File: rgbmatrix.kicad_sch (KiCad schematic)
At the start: 164 parts

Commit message: first
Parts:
- C10: renamed from C2; footprint (none) -> Capacitor_SMD:C_0805_2012Metric_Pad1.18x1.45mm_HandSolder
- C11: renamed from C3; footprint (none) -> Capacitor_SMD:C_0805_2012Metric_Pad1.18x1.45mm_HandSolder
- C12: renamed from C4; footprint (none) -> Capacitor_SMD:C_0805_2012Metric_Pad1.18x1.45mm_HandSolder
- C13: renamed from C5; footprint (none) -> Capacitor_SMD:C_0805_2012Metric_Pad1.18x1.45mm_HandSolder
- C14: renamed from C6; footprint (none) -> Capacitor_SMD:C_0805_2012Metric_Pad1.18x1.45mm_HandSolder
- C15: renamed from C7; footprint (none) -> Capacitor_SMD:C_0805_2012Metric_Pad1.18x1.45mm_HandSolder
- C16: renamed from C8; footprint (none) -> Capacitor_SMD:C_0805_2012Metric_Pad1.18x1.45mm_HandSolder
- C17: renamed from C9; footprint (none) -> Capacitor_SMD:C_0805_2012Metric_Pad1.18x1.45mm_HandSolder
- C18: renamed from C10; footprint (none) -> Capacitor_SMD:C_0805_2012Metric_Pad1.18x1.45mm_HandSolder
- C19: renamed from C11; footprint (none) -> Capacitor_SMD:C_0805_2012Metric_Pad1.18x1.45mm_HandSolder
- C20: renamed from C12; footprint (none) -> Capacitor_SMD:C_0805_2012Metric_Pad1.18x1.45mm_HandSolder
- C21: renamed from C13; footprint (none) -> Capacitor_SMD:C_0805_2012Metric_Pad1.18x1.45mm_HandSolder
- C22: renamed from C14; footprint (none) -> Capacitor_SMD:C_0805_2012Metric_Pad1.18x1.45mm_HandSolder
- C23: renamed from C15; footprint (none) -> Capacitor_SMD:C_0805_2012Metric_Pad1.18x1.45mm_HandSolder
- C24: renamed from C16; footprint (none) -> Capacitor_SMD:C_0805_2012Metric_Pad1.18x1.45mm_HandSolder
- C25: renamed from C17; footprint (none) -> Capacitor_SMD:C_0805_2012Metric_Pad1.18x1.45mm_HandSolder
- C26: renamed from C18; footprint (none) -> Capacitor_SMD:C_0805_2012Metric_Pad1.18x1.45mm_HandSolder
- C27: renamed from C19; footprint (none) -> Capacitor_SMD:C_0805_2012Metric_Pad1.18x1.45mm_HandSolder
- C28: renamed from C20; footprint (none) -> Capacitor_SMD:C_0805_2012Metric_Pad1.18x1.45mm_HandSolder
- C29: renamed from C21; footprint (none) -> Capacitor_SMD:C_0805_2012Metric_Pad1.18x1.45mm_HandSolder
- C30: renamed from C22; footprint (none) -> Capacitor_SMD:C_0805_2012Metric_Pad1.18x1.45mm_HandSolder
- C31: renamed from C23; footprint (none) -> Capacitor_SMD:C_0805_2012Metric_Pad1.18x1.45mm_HandSolder
- C32: renamed from C24; footprint (none) -> Capacitor_SMD:C_0805_2012Metric_Pad1.18x1.45mm_HandSolder
- C33: renamed from C25; footprint (none) -> Capacitor_SMD:C_0805_2012Metric_Pad1.18x1.45mm_HandSolder
- C34: renamed from C26; footprint (none) -> Capacitor_SMD:C_0805_2012Metric_Pad1.18x1.45mm_HandSolder
- C35: renamed from C27; footprint (none) -> Capacitor_SMD:C_0805_2012Metric_Pad1.18x1.45mm_HandSolder
- C36: renamed from C28; footprint (none) -> Capacitor_SMD:C_0805_2012Metric_Pad1.18x1.45mm_HandSolder
- C37: renamed from C29; footprint (none) -> Capacitor_SMD:C_0805_2012Metric_Pad1.18x1.45mm_HandSolder
- C38: renamed from C30; footprint (none) -> Capacitor_SMD:C_0805_2012Metric_Pad1.18x1.45mm_HandSolder
- C39: renamed from C31; footprint (none) -> Capacitor_SMD:C_0805_2012Metric_Pad1.18x1.45mm_HandSolder
- C40: renamed from C32; footprint (none) -> Capacitor_SMD:C_0805_2012Metric_Pad1.18x1.45mm_HandSolder
- C41: renamed from C33; footprint (none) -> Capacitor_SMD:C_0805_2012Metric_Pad1.18x1.45mm_HandSolder
- C42: renamed from C34; footprint (none) -> Capacitor_SMD:C_0805_2012Metric_Pad1.18x1.45mm_HandSolder
- C43: renamed from C35; footprint (none) -> Capacitor_SMD:C_0805_2012Metric_Pad1.18x1.45mm_HandSolder
- C44: renamed from C36; footprint (none) -> Capacitor_SMD:C_0805_2012Metric_Pad1.18x1.45mm_HandSolder
- C45: renamed from C37; footprint (none) -> Capacitor_SMD:C_0805_2012Metric_Pad1.18x1.45mm_HandSolder
- C46: renamed from C38; footprint (none) -> Capacitor_SMD:C_0805_2012Metric_Pad1.18x1.45mm_HandSolder
- C47: renamed from C39; footprint (none) -> Capacitor_SMD:C_0805_2012Metric_Pad1.18x1.45mm_HandSolder
- C48: renamed from C40; footprint (none) -> Capacitor_SMD:C_0805_2012Metric_Pad1.18x1.45mm_HandSolder
- C49: renamed from C41; footprint (none) -> Capacitor_SMD:C_0805_2012Metric_Pad1.18x1.45mm_HandSolder
- C50: renamed from C42; footprint (none) -> Capacitor_SMD:C_0805_2012Metric_Pad1.18x1.45mm_HandSolder
- C51: renamed from C43; footprint (none) -> Capacitor_SMD:C_0805_2012Metric_Pad1.18x1.45mm_HandSolder
- C52: renamed from C44; footprint (none) -> Capacitor_SMD:C_0805_2012Metric_Pad1.18x1.45mm_HandSolder
- C53: renamed from C45; footprint (none) -> Capacitor_SMD:C_0805_2012Metric_Pad1.18x1.45mm_HandSolder
- C54: renamed from C46; footprint (none) -> Capacitor_SMD:C_0805_2012Metric_Pad1.18x1.45mm_HandSolder
- C55: renamed from C47; footprint (none) -> Capacitor_SMD:C_0805_2012Metric_Pad1.18x1.45mm_HandSolder
- C56: renamed from C48; footprint (none) -> Capacitor_SMD:C_0805_2012Metric_Pad1.18x1.45mm_HandSolder
- C57: renamed from C49; footprint (none) -> Capacitor_SMD:C_0805_2012Metric_Pad1.18x1.45mm_HandSolder
- C58: renamed from C50; footprint (none) -> Capacitor_SMD:C_0805_2012Metric_Pad1.18x1.45mm_HandSolder
- C59: renamed from C51; footprint (none) -> Capacitor_SMD:C_0805_2012Metric_Pad1.18x1.45mm_HandSolder
- C60: renamed from C52; footprint (none) -> Capacitor_SMD:C_0805_2012Metric_Pad1.18x1.45mm_HandSolder
- C61: renamed from C53; footprint (none) -> Capacitor_SMD:C_0805_2012Metric_Pad1.18x1.45mm_HandSolder
- C62: renamed from C54; footprint (none) -> Capacitor_SMD:C_0805_2012Metric_Pad1.18x1.45mm_HandSolder
- C63: renamed from C55; footprint (none) -> Capacitor_SMD:C_0805_2012Metric_Pad1.18x1.45mm_HandSolder
- C64: renamed from C56; footprint (none) -> Capacitor_SMD:C_0805_2012Metric_Pad1.18x1.45mm_HandSolder
- C65: renamed from C57; footprint (none) -> Capacitor_SMD:C_0805_2012Metric_Pad1.18x1.45mm_HandSolder
- C66: renamed from C58; footprint (none) -> Capacitor_SMD:C_0805_2012Metric_Pad1.18x1.45mm_HandSolder
- C67: renamed from C59; footprint (none) -> Capacitor_SMD:C_0805_2012Metric_Pad1.18x1.45mm_HandSolder
- C68: renamed from C60; footprint (none) -> Capacitor_SMD:C_0805_2012Metric_Pad1.18x1.45mm_HandSolder
- C69: renamed from C61; footprint (none) -> Capacitor_SMD:C_0805_2012Metric_Pad1.18x1.45mm_HandSolder
- C70: renamed from C62; footprint (none) -> Capacitor_SMD:C_0805_2012Metric_Pad1.18x1.45mm_HandSolder
- C71: renamed from C63; footprint (none) -> Capacitor_SMD:C_0805_2012Metric_Pad1.18x1.45mm_HandSolder
- C72: renamed from C64; footprint (none) -> Capacitor_SMD:C_0805_2012Metric_Pad1.18x1.45mm_HandSolder
- C73: renamed from C65; footprint (none) -> Capacitor_SMD:C_0805_2012Metric_Pad1.18x1.45mm_HandSolder
- C74: renamed from C66; footprint (none) -> Capacitor_SMD:C_0805_2012Metric_Pad1.18x1.45mm_HandSolder
- C75: renamed from C67; footprint (none) -> Capacitor_SMD:C_0805_2012Metric_Pad1.18x1.45mm_HandSolder
- C76: renamed from C68; footprint (none) -> Capacitor_SMD:C_0805_2012Metric_Pad1.18x1.45mm_HandSolder
- C77: renamed from C69; footprint (none) -> Capacitor_SMD:C_0805_2012Metric_Pad1.18x1.45mm_HandSolder
- C78: renamed from C70; footprint (none) -> Capacitor_SMD:C_0805_2012Metric_Pad1.18x1.45mm_HandSolder
- C79: renamed from C71; footprint (none) -> Capacitor_SMD:C_0805_2012Metric_Pad1.18x1.45mm_HandSolder
- C80: renamed from C72; footprint (none) -> Capacitor_SMD:C_0805_2012Metric_Pad1.18x1.45mm_HandSolder
- C81: renamed from C73; footprint (none) -> Capacitor_SMD:C_0805_2012Metric_Pad1.18x1.45mm_HandSolder
- C82: renamed from C74; footprint (none) -> Capacitor_SMD:C_0805_2012Metric_Pad1.18x1.45mm_HandSolder
- C83: renamed from C75; footprint (none) -> Capacitor_SMD:C_0805_2012Metric_Pad1.18x1.45mm_HandSolder
- C84: renamed from C76; footprint (none) -> Capacitor_SMD:C_0805_2012Metric_Pad1.18x1.45mm_HandSolder
- C85: renamed from C77; footprint (none) -> Capacitor_SMD:C_0805_2012Metric_Pad1.18x1.45mm_HandSolder
- C86: renamed from C78; footprint (none) -> Capacitor_SMD:C_0805_2012Metric_Pad1.18x1.45mm_HandSolder
- C87: renamed from C79; footprint (none) -> Capacitor_SMD:C_0805_2012Metric_Pad1.18x1.45mm_HandSolder
- C88: renamed from C80; footprint (none) -> Capacitor_SMD:C_0805_2012Metric_Pad1.18x1.45mm_HandSolder
- C89: renamed from C81; footprint (none) -> Capacitor_SMD:C_0805_2012Metric_Pad1.18x1.45mm_HandSolder
- C9: renamed from C1; footprint (none) -> Capacitor_SMD:C_0805_2012Metric_Pad1.18x1.45mm_HandSolder
- C90: renamed from C82; footprint (none) -> Capacitor_SMD:C_0805_2012Metric_Pad1.18x1.45mm_HandSolder
- renumbered D9 to D10, D10 to D11, D11 to D12, D12 to D13, D13 to D14, D14 to D15, D15 to D16, D16 to D17, D17 to D18, D18 to D19, D1 to D2, D19 to D20, D20 to D21, D21 to D22, D22 to D23, D23 to D24, D24 to D25, D25 to D26, D26 to D27, D27 to D28, D28 to D29, D2 to D3, D29 to D30, D30 to D31, D31 to D32, D32 to D33, D33 to D34, D34 to D35, D35 to D36, D36 to D37, D37 to D38, D38 to D39, D3 to D4, D39 to D40, D40 to D41, D41 to D42, D42 to D43, D43 to D44, D44 to D45, D45 to D46, D46 to D47, D47 to D48, D48 to D49, D4 to D5, D49 to D50, D50 to D51, D51 to D52, D52 to D53, D53 to D54, D54 to D55, D55 to D56, D56 to D57, D57 to D58, D58 to D59, D5 to D6, D59 to D60, D60 to D61, D61 to D62, D62 to D63, D63 to D64, D64 to D65, D65 to D66, D66 to D67, D67 to D68, D68 to D69, D6 to D7, D69 to D70, D70 to D71, D71 to D72, D72 to D73, D73 to D74, D74 to D75, D75 to D76, D76 to D77, D77 to D78, D78 to D79, D7 to D8, D79 to D80, D80 to D81, D81 to D82, D82 to D83, D8 to D9
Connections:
- net +5V: now also D82.2 (VSS), D83.2 (VSS)

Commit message: changed to 60 :C
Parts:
- removed C10, C11, C12, C13, C14, C15, C16, C17, C18, C19, C20, C21, C22, C9: 100nF, Capacitor_SMD:C_0805_2012Metric_Pad1.18x1.45mm_HandSolder, symbol Device:C_Small
- removed D10, D11, D12, D13, D14, D15, D2, D3, D4, D5, D6, D7, D8, D9: SK6812MINI, LED_SMD:LED_SK6812MINI_PLCC4_3.5x3.5mm_P1.75mm, symbol LED:SK6812MINI
- renumbered C24 to C10, C25 to C11, C26 to C12, C27 to C13, C28 to C14, C29 to C15, C30 to C16, C31 to C17, C32 to C18, C33 to C19, C34 to C20, C35 to C21, C36 to C22, C37 to C23, C38 to C24, C39 to C25, C40 to C26, C41 to C27, C42 to C28, C43 to C29, C44 to C30, C45 to C31, C46 to C32, C47 to C33, C48 to C34, C49 to C35, C50 to C36, C51 to C37, C52 to C38, C53 to C39, C54 to C40, C55 to C41, C56 to C42, C57 to C43, C58 to C44, C59 to C45, C60 to C46, C61 to C47, C62 to C48, C63 to C49, C64 to C50, C65 to C51, C66 to C52, C67 to C53, C68 to C54, C69 to C55, C70 to C56, C71 to C57, C72 to C58, C73 to C59, C74 to C60, C75 to C61, C76 to C62, C77 to C63, C78 to C64, C79 to C65, C80 to C66, C81 to C67, C82 to C68, C83 to C69, C84 to C70, C85 to C71, C86 to C72, C87 to C73, C88 to C74, C89 to C75, C90 to C76, C23 to C9, D24 to D10, D25 to D11, D26 to D12, D27 to D13, D28 to D14, D29 to D15, D30 to D16, D31 to D17, D32 to D18, D33 to D19, D16 to D2, D34 to D20, D35 to D21, D36 to D22, D37 to D23, D38 to D24, D39 to D25, D40 to D26, D41 to D27, D42 to D28, D43 to D29, D17 to D3, D44 to D30, D45 to D31, D46 to D32, D47 to D33, D48 to D34, D49 to D35, D50 to D36, D51 to D37, D52 to D38, D53 to D39, D18 to D4, D54 to D40, D55 to D41, D56 to D42, D57 to D43, D58 to D44, D59 to D45, D60 to D46, D61 to D47, D62 to D48, D63 to D49, D19 to D5, D64 to D50, D65 to D51, D66 to D52, D67 to D53, D68 to D54, D69 to D55, D70 to D56, D71 to D57, D72 to D58, D73 to D59, D20 to D6, D74 to D60, D75 to D61, D76 to D62, D77 to D63, D78 to D64, D79 to D65, D80 to D66, D81 to D67, D82 to D68, D83 to D69, D21 to D7, D22 to D8, D23 to D9
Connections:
- net D72 is gone; now on net D59: D59.1 (DOUT), D60.3 (DIN)
- net D59: no longer D46.3 (DIN)
- net D14 renamed LED
- net D29 renamed D16
- net D44 renamed D31
- net D58 renamed D45
- net D45: now also D46.3 (DIN)
- net D80: no longer names the net of D67.1 (DOUT), D68.3 (DIN)
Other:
- moved on the sheet: C10, C11, C12, C13, C14, C15, C16, C17, C18, C19, C20, C21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

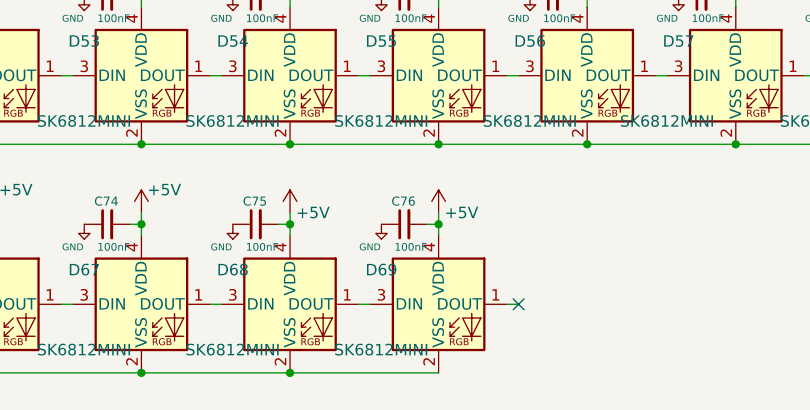
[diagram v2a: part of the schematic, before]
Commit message: moved keys/neopixels
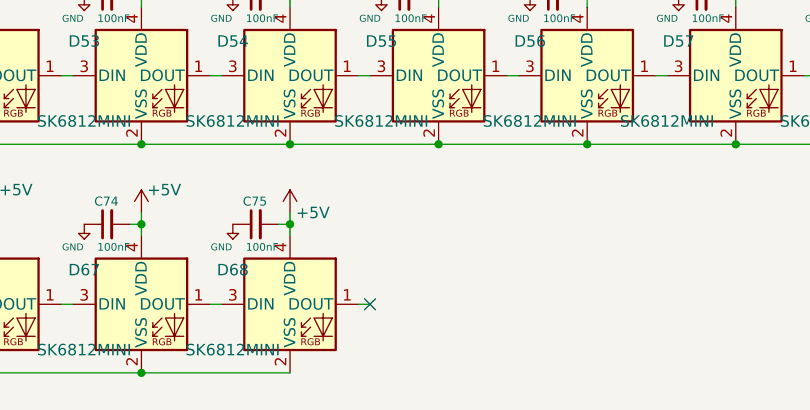
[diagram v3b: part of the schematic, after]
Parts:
- removed C76: 100nF, Capacitor_SMD:C_0805_2012Metric_Pad1.18x1.45mm_HandSolder, symbol Device:C_Small
- removed D69: SK6812MINI, LED_SMD:LED_SK6812MINI_PLCC4_3.5x3.5mm_P1.75mm, symbol LED:SK6812MINI
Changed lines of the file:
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@@
   (junction (at 49.53 69.85) (diameter 0) (color 0 0 0 0)
   )
-  (junction (at 165.1 147.32) (diameter 0) (color 0 0 0 0)
-  )
   (junction (at 49.53 24.13) (diameter 0) (color 0 0 0 0)
   )
@@
   (junction (at 66.04 96.52) (diameter 0) (color 0 0 0 0)
   )
-  (junction (at 181.61 130.81) (diameter 0) (color 0 0 0 0)
-  )
   (junction (at 148.59 40.64) (diameter 0) (color 0 0 0 0)
   )
@@
   (junction (at 214.63 24.13) (diameter 0) (color 0 0 0 0)
   )
-  (no_connect (at 190.5 139.7))
+  (no_connect (at 173.99 139.7))
   (wire (pts (xy 49.53 52.07) (xy 49.53 53.34))
     (stroke (width 0) (type default) (color 0 0 0 0))
@@
     (stroke (width 0) (type default) (color 0 0 0 0))
   )
-  (wire (pts (xy 165.1 147.32) (xy 181.61 147.32))
-    (stroke (width 0) (type default) (color 0 0 0 0))
-  )
   (wire (pts (xy 115.57 22.86) (xy 115.57 24.13))
     (stroke (width 0) (type default) (color 0 0 0 0))
@@
     (stroke (width 0) (type default) (color 0 0 0 0))
   )
-  (wire (pts (xy 180.34 130.81) (xy 181.61 130.81))
-    (stroke (width 0) (type default) (color 0 0 0 0))
-  )
-  (wire (pts (xy 181.61 129.54) (xy 181.61 130.81))
-    (stroke (width 0) (type default) (color 0 0 0 0))
-  )
   (wire (pts (xy 246.38 80.01) (xy 247.65 80.01))
     (stroke (width 0) (type default) (color 0 0 0 0))
@@
     (stroke (width 0) (type default) (color 0 0 0 0))
   )
-  (wire (pts (xy 181.61 130.81) (xy 181.61 132.08))
-    (stroke (width 0) (type default) (color 0 0 0 0))
-  )
   (wire (pts (xy 49.53 147.32) (xy 58.42 147.32))
     (stroke (width 0) (type default) (color 0 0 0 0))
@@
     (stroke (width 0) (type default) (color 0 0 0 0))
   )
-  (wire (pts (xy 189.23 139.7) (xy 190.5 139.7))
-    (stroke (width 0) (type default) (color 0 0 0 0))
-  )
   (wire (pts (xy 247.65 52.07) (xy 247.65 53.34))
     (stroke (width 0) (type default) (color 0 0 0 0))
@@
     (pin "1")
   )
-  (symbol (lib_id "keyboard_parts:GND") (at 175.26 130.81 0) (unit 1)
-    (in_bom yes) (on_board yes)
-    (property "Reference" "#PWR0157" (id 0) (at 175.26 129.54 0)
-      (effects (font (size 0.508 0.508)) hide)
-    )
-    (property "Value" "GND" (id 1) (at 173.99 133.35 0)
-      (effects (font (size 0.762 0.762)))
-    )
-    (property "Footprint" "" (id 2) (at 175.26 130.81 0)
-      (effects (font (size 1.524 1.524)))
-    )
-    (property "Datasheet" "" (id 3) (at 175.26 130.81 0)
-      (effects (font (size 1.524 1.524)))
-    )
-    (pin "1")
-  )
   (symbol (lib_id "Device:C_Small") (at 161.29 24.13 90) (unit 1)
     (in_bom yes) (on_board yes)
@@
     (pin "4")
   )
-  (symbol (lib_id "Device:C_Small") (at 177.8 130.81 90) (unit 1)
-    (in_bom yes) (on_board yes)
-    (property "Reference" "C76" (id 0) (at 179.07 128.27 90)
-      (effects (font (size 1 1)) (justify left))
-    )
-    (property "Value" "100nF" (id 1) (at 180.34 133.35 90)
-      (effects (font (size 0.85 0.85)) (justify left))
-    )
-    (property "Footprint" "Capacitor_SMD:C_0805_2012Metric_Pad1.18x1.45mm_HandSolder" (id 2) (at 177.8 130.81 0)
-      (effects (font (size 1.27 1.27)) hide)
-    )
-    (property "Datasheet" "~" (id 3) (at 177.8 130.81 0)
-      (effects (font (size 1.27 1.27)) hide)
-    )
-    (pin "1")
-    (pin "2")
-  )
   (symbol (lib_id "keyboard_parts:GND") (at 241.3 53.34 0) (unit 1)
     (in_bom yes) (on_board yes)
@@
     (pin "1")
   )
-  (symbol (lib_id "power:+5V") (at 181.61 129.54 0) (unit 1)
-    (in_bom yes) (on_board yes)
-    (property "Reference" "#PWR0147" (id 0) (at 181.61 133.35 0)
-      (effects (font (size 1.27 1.27)) hide)
-    )
-    (property "Value" "+5V" (id 1) (at 184.15 129.54 0))
-    (property "Footprint" "" (id 2) (at 181.61 129.54 0)
-      (effects (font (size 1.27 1.27)) hide)
-    )
-    (property "Datasheet" "" (id 3) (at 181.61 129.54 0)
-      (effects (font (size 1.27 1.27)) hide)
-    )
-    (pin "1")
-  )
   (symbol (lib_id "Device:C_Small") (at 29.21 24.13 90) (unit 1)
     (in_bom yes) (on_board yes)
@@
     (pin "1")
   )
-  (symbol (lib_id "LED:SK6812MINI") (at 181.61 139.7 0) (unit 1)
-    (in_bom yes) (on_board yes)
-    (property "Reference" "D69" (id 0) (at 175.26 135.89 0))
-    (property "Value" "SK6812MINI" (id 1) (at 175.26 144.78 0))
-    (property "Footprint" "LED_SMD:LED_SK6812MINI_PLCC4_3.5x3.5mm_P1.75mm" (id 2) (at 182.88 147.32 0)
-      (effects (font (size 1.27 1.27)) (justify left top) hide)
-    )
-    (property "Datasheet" "https://cdn-shop.adafruit.com/product-files/2686/SK6812MINI_REV.01-1-2.pdf" (id 3) (at 184.15 149.225 0)
-      (effects (font (size 1.27 1.27)) (justify left top) hide)
-    )
-    (pin "1")
-    (pin "2")
-    (pin "3")
-    (pin "4")
-  )
   (symbol (lib_id "Device:C_Small") (at 111.76 105.41 90) (unit 1)

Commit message: began routing for real
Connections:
- net +5V: no longer C10.1, C11.1, C12.1, C13.1, C14.1, C15.1, C16.1, C17.1, C18.1, C19.1, C20.1, C21.1, C22.1, C23.1, C24.1, C25.1, C26.1, C27.1, C28.1, C29.1, C30.1, C31.1, C32.1, C33.1, C34.1, C35.1, C36.1, C37.1, C38.1, C39.1, C40.1, C41.1, C42.1, C43.1, C44.1, C45.1, C46.1, C47.1, C48.1, C49.1, C50.1, C51.1, C52.1, C53.1, C54.1, C55.1, C56.1, C57.1, C58.1, C59.1, C60.1, C61.1, C62.1, C63.1, C64.1, C65.1, C66.1, C67.1, C68.1, C69.1, C70.1, C71.1, C72.1, C73.1, C74.1, C75.1, C9.1, D10.2 (VSS), D11.2 (VSS), D12.2 (VSS), D13.2 (VSS), D14.2 (VSS), D15.2 (VSS), D16.2 (VSS), D17.2 (VSS), D18.2 (VSS), D19.2 (VSS), D2.2 (VSS), D20.2 (VSS), D21.2 (VSS), D22.2 (VSS), D23.2 (VSS), D24.2 (VSS), D25.2 (VSS), D26.2 (VSS), D27.2 (VSS), D28.2 (VSS), D29.2 (VSS), D3.2 (VSS), D30.2 (VSS), D31.2 (VSS), D32.2 (VSS), D33.2 (VSS), D34.2 (VSS), D35.2 (VSS), D36.2 (VSS), D37.2 (VSS), D38.2 (VSS), D39.2 (VSS), D4.2 (VSS), D40.2 (VSS), D41.2 (VSS), D42.2 (VSS), D43.2 (VSS), D44.2 (VSS), D45.2 (VSS), D46.2 (VSS), D47.2 (VSS), D48.2 (VSS), D49.2 (VSS), D5.2 (VSS), D50.2 (VSS), D51.2 (VSS), D52.2 (VSS), D53.2 (VSS), D54.2 (VSS), D55.2 (VSS), D56.2 (VSS), D57.2 (VSS), D58.2 (VSS), D59.2 (VSS), D6.2 (VSS), D60.2 (VSS), D61.2 (VSS), D62.2 (VSS), D63.2 (VSS), D64.2 (VSS), D65.2 (VSS), D66.2 (VSS), D67.2 (VSS), D68.2 (VSS), D7.2 (VSS), D8.2 (VSS), D9.2 (VSS)
- new net GND: C10.1, C11.1, C12.1, C13.1, C14.1, C15.1, C16.1, C17.1, C18.1, C19.1, C20.1, C21.1, C22.1, C23.1, C24.1, C25.1, C26.1, C27.1, C28.1, C29.1, C30.1, C31.1, C32.1, C33.1, C34.1, C35.1, C36.1, C37.1, C38.1, C39.1, C40.1, C41.1, C42.1, C43.1, C44.1, C45.1, C46.1, C47.1, C48.1, C49.1, C50.1, C51.1, C52.1, C53.1, C54.1, C55.1, C56.1, C57.1, C58.1, C59.1, C60.1, C61.1, C62.1, C63.1, C64.1, C65.1, C66.1, C67.1, C68.1, C69.1, C70.1, C71.1, C72.1, C73.1, C74.1, C75.1, C9.1, D10.2 (VSS), D11.2 (VSS), D12.2 (VSS), D13.2 (VSS), D14.2 (VSS), D15.2 (VSS), D16.2 (VSS), D17.2 (VSS), D18.2 (VSS), D19.2 (VSS), D2.2 (VSS), D20.2 (VSS), D21.2 (VSS), D22.2 (VSS), D23.2 (VSS), D24.2 (VSS), D25.2 (VSS), D26.2 (VSS), D27.2 (VSS), D28.2 (VSS), D29.2 (VSS), D3.2 (VSS), D30.2 (VSS), D31.2 (VSS), D32.2 (VSS), D33.2 (VSS), D34.2 (VSS), D35.2 (VSS), D36.2 (VSS), D37.2 (VSS), D38.2 (VSS), D39.2 (VSS), D4.2 (VSS), D40.2 (VSS), D41.2 (VSS), D42.2 (VSS), D43.2 (VSS), D44.2 (VSS), D45.2 (VSS), D46.2 (VSS), D47.2 (VSS), D48.2 (VSS), D49.2 (VSS), D5.2 (VSS), D50.2 (VSS), D51.2 (VSS), D52.2 (VSS), D53.2 (VSS), D54.2 (VSS), D55.2 (VSS), D56.2 (VSS), D57.2 (VSS), D58.2 (VSS), D59.2 (VSS), D6.2 (VSS), D60.2 (VSS), D61.2 (VSS), D62.2 (VSS), D63.2 (VSS), D64.2 (VSS), D65.2 (VSS), D66.2 (VSS), D67.2 (VSS), D68.2 (VSS), D7.2 (VSS), D8.2 (VSS), D9.2 (VSS)

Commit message: fked up LEDs :C
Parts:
- D10, D11, D12, D13, D14, D15, D16, D17, D18, D19, D2, D20, D21, D22, D23, D24, D25, D26, D27, D28, D29, D3, D30, D31, D32, D33, D34, D35, D36, D37, D38, D39, D4, D40, D41, D42, D43, D44, D45, D46, D47, D48, D49, D5, D50, D51, D52, D53, D54, D55, D56, D57, D58, D59, D6, D60, D61, D62, D63, D64, D65, D66, D67, D68, D7, D8, D9: footprint LED_SMD:LED_SK6812MINI_PLCC4_3.5x3.5mm_P1.75mm -> reverse:MX_SK6812MINI-E_REV

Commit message: pensive
changed LEDs aaaAAAAAAA
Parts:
- removed C23: 100nF, Capacitor_SMD:C_0805_2012Metric_Pad1.18x1.45mm_HandSolder, symbol Device:C_Small
- removed D16: SK6812MINI, reverse:MX_SK6812MINI-E_REV, symbol LED:SK6812MINI
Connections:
- net D16: now also D15.1 (DOUT)
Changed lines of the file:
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@@
   (junction (at 214.63 105.41) (diameter 0) (color 0 0 0 0)
   )
-  (junction (at 247.65 40.64) (diameter 0) (color 0 0 0 0)
-  )
   (junction (at 66.04 69.85) (diameter 0) (color 0 0 0 0)
   )
@@
   (junction (at 231.14 24.13) (diameter 0) (color 0 0 0 0)
   )
-  (junction (at 264.16 24.13) (diameter 0) (color 0 0 0 0)
-  )
   (junction (at 132.08 96.52) (diameter 0) (color 0 0 0 0)
   )
@@
     (stroke (width 0) (type default) (color 0 0 0 0))
   )
-  (wire (pts (xy 264.16 24.13) (xy 264.16 25.4))
-    (stroke (width 0) (type default) (color 0 0 0 0))
-  )
   (wire (pts (xy 49.53 22.86) (xy 49.53 24.13))
     (stroke (width 0) (type default) (color 0 0 0 0))
@@
     (stroke (width 0) (type default) (color 0 0 0 0))
   )
-  (wire (pts (xy 247.65 40.64) (xy 264.16 40.64))
-    (stroke (width 0) (type default) (color 0 0 0 0))
-  )
   (wire (pts (xy 198.12 80.01) (xy 198.12 81.28))
     (stroke (width 0) (type default) (color 0 0 0 0))
@@
     (stroke (width 0) (type default) (color 0 0 0 0))
   )
-  (wire (pts (xy 264.16 22.86) (xy 264.16 24.13))
-    (stroke (width 0) (type default) (color 0 0 0 0))
-  )
   (wire (pts (xy 148.59 69.85) (xy 165.1 69.85))
     (stroke (width 0) (type default) (color 0 0 0 0))
@@
     (stroke (width 0) (type default) (color 0 0 0 0))
   )
-  (wire (pts (xy 262.89 24.13) (xy 264.16 24.13))
-    (stroke (width 0) (type default) (color 0 0 0 0))
-  )
   (wire (pts (xy 165.1 69.85) (xy 181.61 69.85))
     (stroke (width 0) (type default) (color 0 0 0 0))
@@
     )
   )
-  (global_label "D16" (shape input) (at 271.78 33.02 0) (fields_autoplaced)
+  (global_label "D16" (shape input) (at 256.54 33.02 0) (fields_autoplaced)
     (effects (font (size 1.27 1.27)) (justify left))
-    (property "Intersheet References" "${INTERSHEET_REFS}" (id 0) (at 277.8821 32.9406 0)
+    (property "Intersheet References" "${INTERSHEET_REFS}" (id 0) (at 262.6421 32.9406 0)
       (effects (font (size 1.27 1.27)) (justify left) hide)
     )
@@
     (pin "2")
   )
-  (symbol (lib_id "Device:C_Small") (at 260.35 24.13 90) (unit 1)
-    (in_bom yes) (on_board yes)
-    (property "Reference" "C23" (id 0) (at 261.62 21.59 90)
-      (effects (font (size 1 1)) (justify left))
-    )
-    (property "Value" "100nF" (id 1) (at 262.89 26.67 90)
-      (effects (font (size 0.85 0.85)) (justify left))
-    )
-    (property "Footprint" "Capacitor_SMD:C_0805_2012Metric_Pad1.18x1.45mm_HandSolder" (id 2) (at 260.35 24.13 0)
-      (effects (font (size 1.27 1.27)) hide)
-    )
-    (property "Datasheet" "~" (id 3) (at 260.35 24.13 0)
-      (effects (font (size 1.27 1.27)) hide)
-    )
-    (pin "1")
-    (pin "2")
-  )
   (symbol (lib_id "power:+5V") (at 115.57 104.14 0) (unit 1)
     (in_bom yes) (on_board yes)
@@
     (pin "2")
   )
-  (symbol (lib_id "LED:SK6812MINI") (at 264.16 33.02 0) (unit 1)
-    (in_bom yes) (on_board yes)
-    (property "Reference" "D16" (id 0) (at 257.81 29.21 0))
-    (property "Value" "SK6812MINI" (id 1) (at 257.81 38.1 0))
-    (property "Footprint" "reverse:MX_SK6812MINI-E_REV" (id 2) (at 265.43 40.64 0)
-      (effects (font (size 1.27 1.27)) (justify left top) hide)
-    )
-    (property "Datasheet" "https://cdn-shop.adafruit.com/product-files/2686/SK6812MINI_REV.01-1-2.pdf" (id 3) (at 266.7 42.545 0)
-      (effects (font (size 1.27 1.27)) (justify left top) hide)
-    )
-    (pin "1")
-    (pin "2")
-    (pin "3")
-    (pin "4")
-  )
   (symbol (lib_id "power:+5V") (at 49.53 78.74 0) (unit 1)
     (in_bom yes) (on_board yes)
@@
     (pin "2")
   )
-  (symbol (lib_id "power:+5V") (at 264.16 22.86 0) (unit 1)
-    (in_bom yes) (on_board yes)
-    (property "Reference" "#PWR032" (id 0) (at 264.16 26.67 0)
-      (effects (font (size 1.27 1.27)) hide)
-    )
-    (property "Value" "+5V" (id 1) (at 266.7 20.32 0))
-    (property "Footprint" "" (id 2) (at 264.16 22.86 0)
-      (effects (font (size 1.27 1.27)) hide)
-    )
-    (property "Datasheet" "" (id 3) (at 264.16 22.86 0)
-      (effects (font (size 1.27 1.27)) hide)
-    )
-    (pin "1")
-  )
   (symbol (lib_id "LED:SK6812MINI") (at 165.1 114.3 0) (unit 1)
     (in_bom yes) (on_board yes)
@@
     (pin "2")
   )
-  (symbol (lib_id "power:GND") (at 257.81 24.13 0) (unit 1)
-    (in_bom yes) (on_board yes)
-    (property "Reference" "#PWR0173" (id 0) (at 257.81 30.48 0)
-      (effects (font (size 1.27 1.27)) hide)
-    )
-    (property "Value" "GND" (id 1) (at 256.54 26.67 0)
-      (effects (font (size 0.762 0.762)))
-    )
-    (property "Footprint" "" (id 2) (at 257.81 24.13 0)
-      (effects (font (size 1.27 1.27)) hide)
-    )
-    (property "Datasheet" "" (id 3) (at 257.81 24.13 0)
-      (effects (font (size 1.27 1.27)) hide)
-    )
-    (pin "1")
-  )
   (symbol (lib_id "LED:SK6812MINI") (at 198.12 33.02 0) (unit 1)
